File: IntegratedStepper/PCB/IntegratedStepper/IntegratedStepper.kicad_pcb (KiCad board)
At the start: 2 copper layers, 42 x 42 mm, 82 parts, among them IC1 DRV8844PWPR, IC2 SN65HVD230DR, IC3 LMR38020FSQDDARQ1, J1 8P8C, J2 8P8C, J3 Screw_Terminal_01x02, J4 Screw_Terminal_01x02, J5 Conn_01x05_Socket, P1 USB_C_Plug, Q1 SS8050-G, Q2 SS8050-G, U1 ESP32-WROOM-32E, U2 AS5048A, U3 CP2102N-Axx-xQFN28

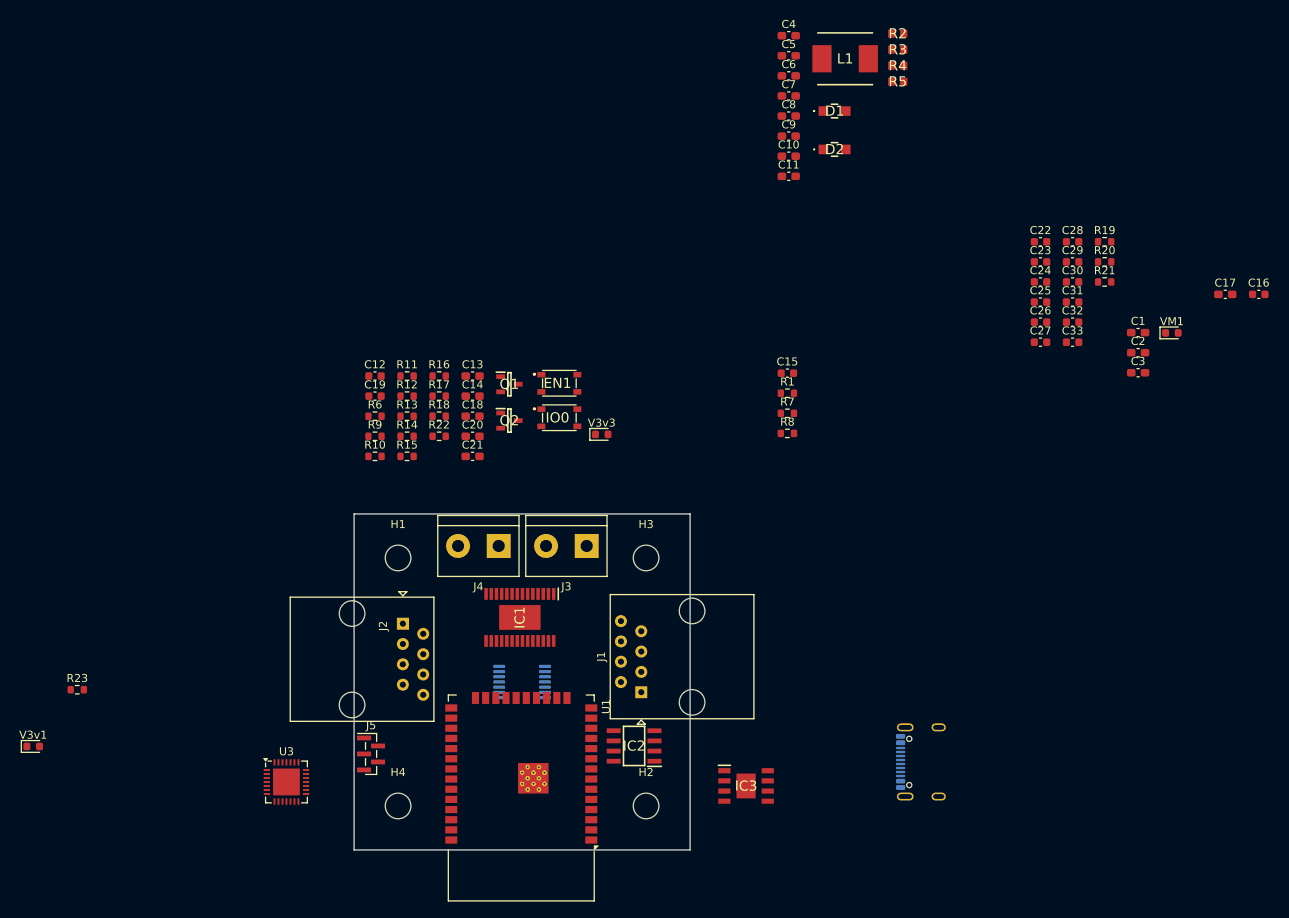
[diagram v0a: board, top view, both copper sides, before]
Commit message: Add intermediate layout + routing to integrated stepper
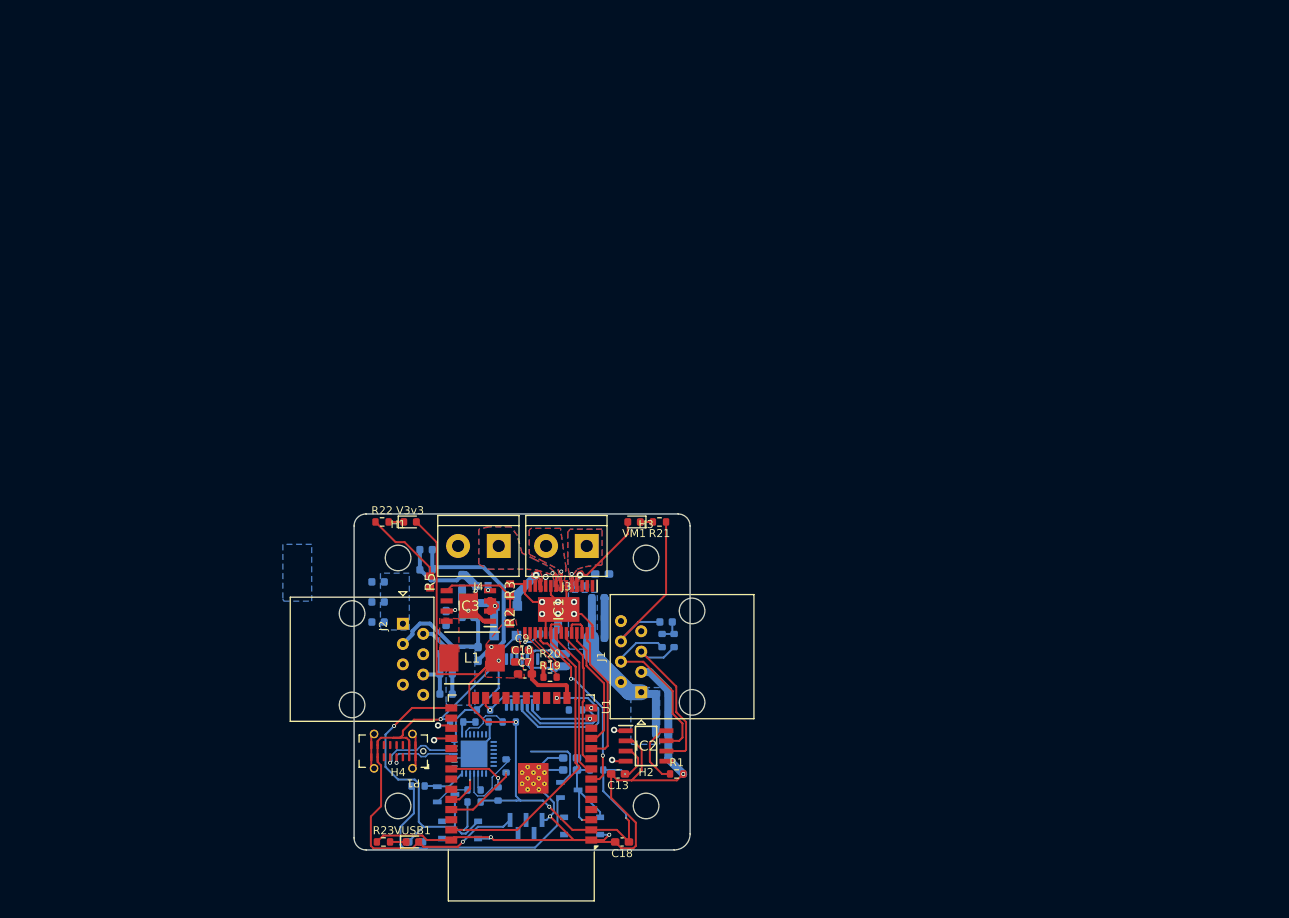
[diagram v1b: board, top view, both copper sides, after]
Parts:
- C1, C11, C12, C14, C15, C16, C17, C19, C2, C20, C21, C22, C23, C24, C25, C26, C27, C28, C29, C3, C30, C31, C32, C33, C4, C5, C6, C8, D1, D2, EN1, IO0, J5, Q1, Q2, R10, R11, R12, R13, R14, R15, R16, R17, R18, R4, R6, R7, R8, R9, U3: moved to B.Cu
- P1: footprint Connector_USB:USB_C_Receptacle_GCT_USB4105-xx-A_16P_TopMnt_Horizontal -> Connector_USB:USB_C_Receptacle_G-Switch_GT-USB-7051x; moved to F.Cu
- moved C16 97.9 mm to (126.5, 118.3), turned to 90 degrees
- moved C17 95.6 mm to (125.0, 118.4), turned to 90 degrees
- moved C31 93.6 mm to (103.0, 108.5), turned to 180 degrees
- moved C32 93.6 mm to (103.0, 111.0), turned to 180 degrees
- moved C33 93.6 mm to (103.0, 113.5), turned to 180 degrees
- moved L1 88.2 mm to (114.8, 118.0)
- moved R19 88.1 mm to (124.5, 120.4)
- moved R2 87.6 mm to (119.5, 113.0), turned to 90 degrees
- moved C26 86.3 mm to (111.5, 120.0), turned to 180 degrees
- moved C27 86.3 mm to (111.5, 122.5), turned to 180 degrees
- moved C25 86.3 mm to (111.5, 117.5), turned to 180 degrees
- moved R20 85.7 mm to (124.5, 118.9)
- moved R5 85.6 mm to (109.5, 108.5), turned to 90 degrees
- moved R4 83.2 mm to (116.0, 109.0), turned to 180 degrees
- moved R3 83.1 mm to (119.5, 109.5), turned to 90 degrees
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- renumbered V3v1 to VUSB1
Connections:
- net /CAN_Transciever/RX renamed /CAN_Transciever/CAN_RX
- net /CAN_Transciever/TX renamed /CAN_Transciever/CAN_TX
- C10 pad 2: VS -> GND
- C22 pad 2: VS -> GND
- C23 pad 2: VS -> GND
- C24 pad 2: VS -> GND
- C25 pad 2: VS -> GND
- C26 pad 2: VS -> GND
- C27 pad 2: VS -> GND
- C28 pad 2: VS -> GND
- C29 pad 2: VS -> GND
- C3 pad 1: VS -> GND
- C30 pad 2: VS -> GND
- C31 pad 2: VS -> GND
- C32 pad 2: VS -> GND
- C33 pad 2: VS -> GND
- C4 pad 1: VS -> GND
- C5 pad 1: VS -> GND
- C6 pad 1: VS -> GND
- C7 pad 2: VS -> GND
- C8 pad 2: VS -> GND
- C9 pad 2: VS -> GND
- IC1 pad 14: VS -> GND
- IC1 pad 28: VS -> GND
- IC1 pad 29: VS -> GND
- IC1 pad 6: VS -> GND
- IC1 pad 9: VS -> GND
- IC3 pad 1: VS -> GND
- IC3 pad 9: VS -> GND
- J1 pad 3: VS -> GND
- J1 pad 6: VS -> GND
- J2 pad 3: VS -> GND
- J2 pad 6: VS -> GND
- R21 pad 1: VS -> GND
- R3 pad 2: VS -> GND
- R4 pad 2: VS -> GND
- R5 pad 2: VS -> GND
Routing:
- net GND: track 0.00 -> 253.1 mm, vias 0 -> 13
- net 3V3_VCC: track 0.00 -> 135.1 mm, vias 0 -> 6
- net /3V3_VReg/V_USB: track 0.00 -> 62.6 mm, vias 0 -> 2
- net VCC: track 0.00 -> 57.3 mm, vias 0 -> 2
- net CANH: track 0.00 -> 53.6 mm
- net CANL: track 0.00 -> 48.6 mm
- net /DRV8844/EN3: track 0.00 -> 44.5 mm, vias 0 -> 1
- net IO0: track 0.00 -> 38.9 mm, vias 0 -> 1
- net Net-(Q1-B): track 0.00 -> 32.8 mm
- net /CAN_Transciever/CAN_RX: track 0.00 -> 29.3 mm, vias 0 -> 2
- net /CAN_Transciever/CAN_TX: track 0.00 -> 25.5 mm, vias 0 -> 2
- net /DRV8844/NFAULT: track 0.00 -> 23.2 mm, vias 0 -> 2
- net /DRV8844/IN4: track 0.00 -> 19.2 mm
- net /ESP32_MCU/M_MOSI: track 0.00 -> 18.8 mm, vias 0 -> 1
- net /DRV8844/IN3: track 0.00 -> 17.5 mm
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- added copper zone on B.Cu, net /DRV8844/OUT1
- added copper zone on F.Cu, net /DRV8844/OUT1
- added copper zone on B.Cu, net /DRV8844/OUT2
- added copper zone on F.Cu, net /DRV8844/OUT2
- added copper zone on B.Cu, net /DRV8844/OUT3
- added copper zone on F.Cu, net /DRV8844/OUT3
- added copper zone on In1.Cu, net /DRV8844/OUT4
- added copper zone on In2.Cu, net /DRV8844/OUT4
- added copper zone on F.Cu, net 3V3_VCC
- added copper zone on F.Cu, net Net-(IC3-SW)
- added copper zone on B.Cu, net VCC
- added copper zone on F.Cu, net VCC
- added copper zone on In1.Cu, net VCC
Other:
- outline, holes or cut-outs redrawn
- copper layers 2 -> 4

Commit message: Add final layout + 3D models
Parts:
- removed P1: USB_C_Plug, Connector_USB:USB_C_Receptacle_G-Switch_GT-USB-7051x
- added USBC1: TYPE-C 3.1_C168690, easyeda2kicad:USB-C-SMD_TYPE-C-USB-3, F.Cu at (104.9, 129.8)
- moved R17 1.25 mm to (119.2, 135.0)
- moved R11 0.25 mm to (119.2, 131.5)
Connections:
- net /3V3_VReg/V_USB renamed V_USB
- IC1 pad 24: /DRV8844/EN1 -> /DRV8844/EN2
- IC1 pad 26: /DRV8844/EN1 -> /DRV8844/EN2
- R17 pad 2: /DRV8844/EN1 -> /DRV8844/EN3
- R18 pad 2: /DRV8844/EN3 -> /DRV8844/EN2
- U1 pad 31: /DRV8844/EN1 -> /DRV8844/EN3
- U1 pad 37: /DRV8844/EN3 -> /DRV8844/EN2
- U3 pad 4: /ESP32_MCU/USB_D+ -> USB_D+
- U3 pad 5: /ESP32_MCU/USB_D- -> USB_D-
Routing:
- net /DRV8844/EN2: track 0.00 -> 47.4 mm, vias 0 -> 3
- net GND: track 253.1 -> 289.7 mm, vias 13 -> 16
- net /ESP32_MCU/ENC_IND: track 0.00 -> 23.5 mm, vias 0 -> 1
- net /ESP32_MCU/ENC-: track 0.00 -> 23.2 mm, vias 0 -> 1
- net /ESP32_MCU/ENC+: track 0.00 -> 19.3 mm, vias 0 -> 3
- net RTS: track 11.4 -> 23.0 mm
- net USB_D+: track 0.00 -> 11.2 mm, vias 0 -> 1
- net /DRV8844/EN1: track 10.8 -> 0.00 mm, vias 1 -> 0
- net USB_D-: track 0.00 -> 10.5 mm, vias 0 -> 2
- net /ESP32_MCU/USB_D-: track 9.60 -> 0.00 mm, vias 1 -> 0
- net /DRV8844/EN3: track 44.5 -> 35.7 mm
- net /ESP32_MCU/USB_D+: track 8.50 -> 0.00 mm, vias 1 -> 0
- net IO0: track 38.9 -> 44.0 mm
- net 3V3_VCC: track 135.1 -> 138.6 mm, vias 6 -> 7
- net Net-(IC3-PG): track 0.00 -> 3.01 mm, vias 0 -> 2
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- added copper zone on In1.Cu, net 3V3_VCC
- added copper zone on B.Cu, net GND
- added copper zone on F.Cu, net GND
- added copper zone on In2.Cu, net GND
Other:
- board size 42 x 42 mm -> 42 x 42.5 mm

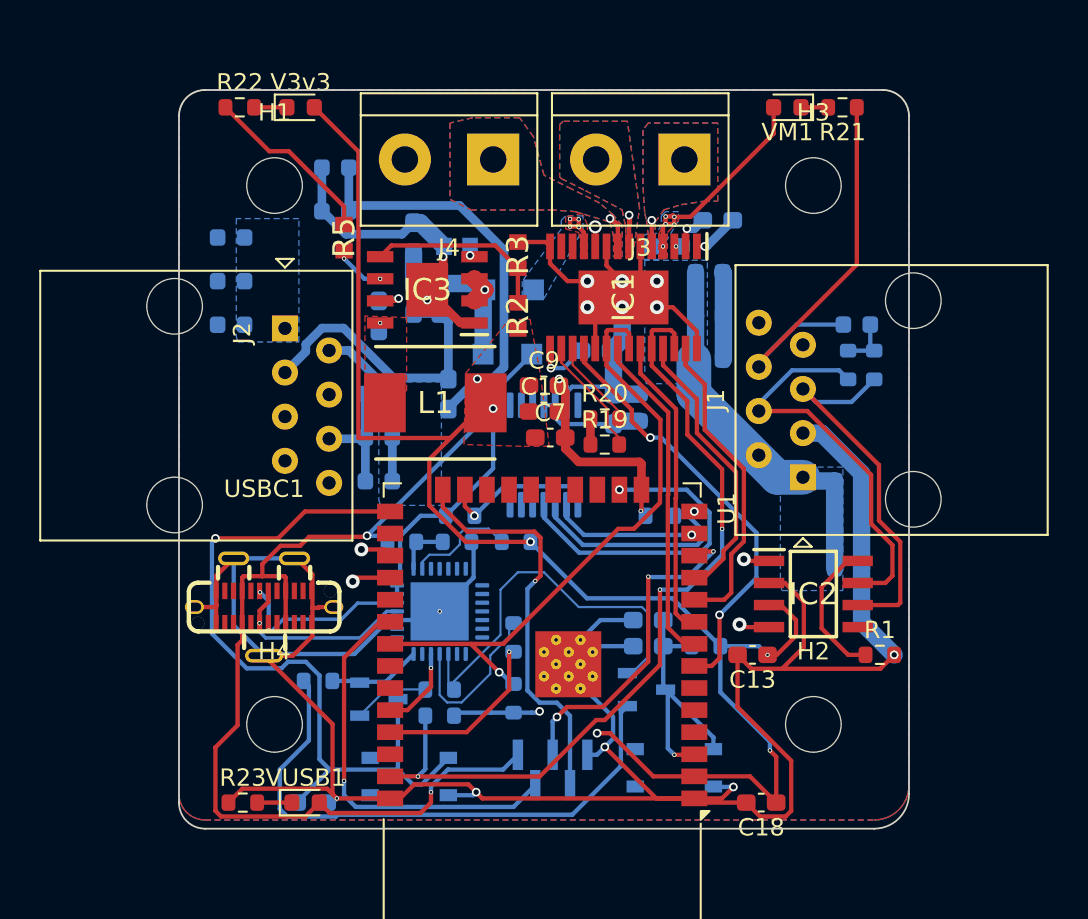
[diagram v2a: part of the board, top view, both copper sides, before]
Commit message: add changes for instock parts
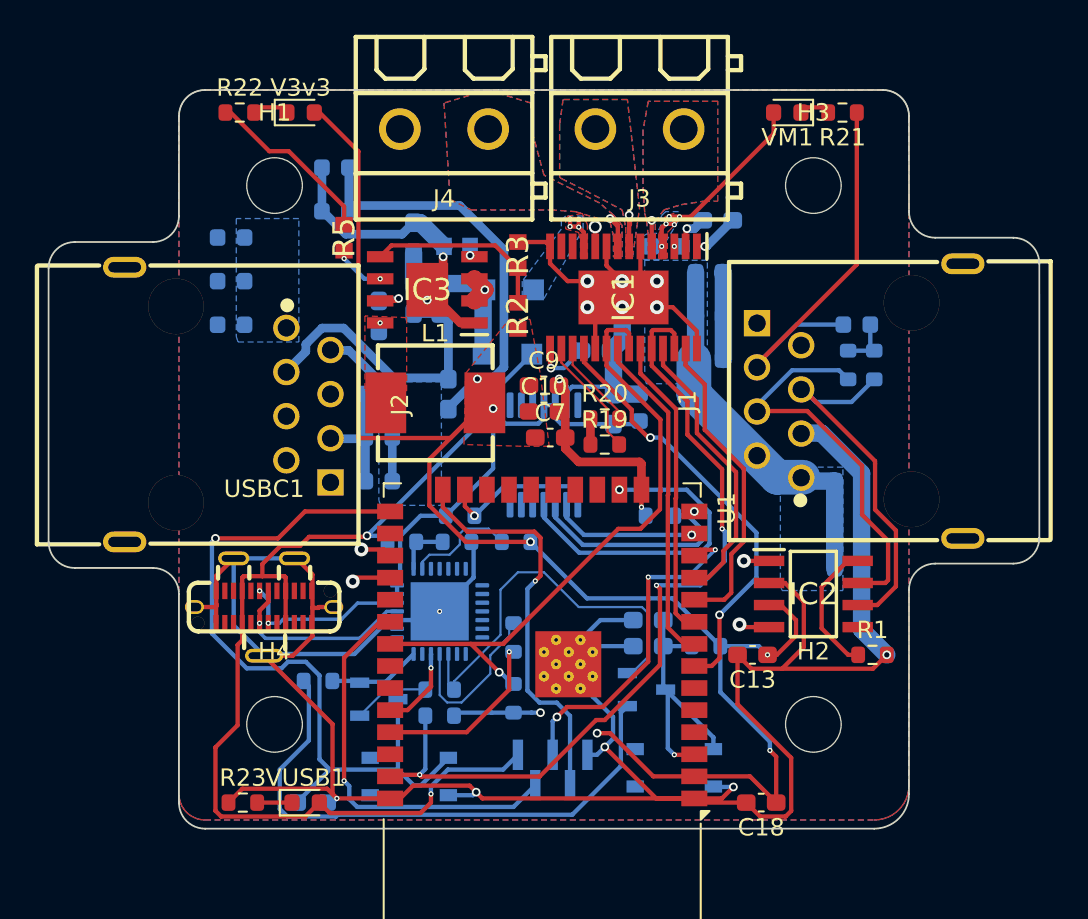
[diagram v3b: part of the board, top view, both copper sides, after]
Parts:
- J1, J2: footprint Connector_RJ:RJ45_Amphenol_54602-x08_Horizontal -> easyeda2kicad:RJ45-TH_KH-RJ45-58-8P8C
- J3, J4: footprint TerminalBlock:TerminalBlock_bornier-2_P5.08mm -> easyeda2kicad:CONN-TH_P5.08_KF128-5.08-2P
- L1: footprint SamacSys_Parts:INDPM6965X300N -> easyeda2kicad:IND-SMD_L7.2-W6.6_GPSR07X0
- moved J2 5.49 mm to (102.8, 118.1)
- moved J1 5.47 mm to (139.2, 117.9)
- moved J4 3.33 mm to (115.2, 102.2)
- moved J3 3.12 mm to (126.5, 102.2)
- moved R1 0.42 mm to (139.9, 132.5)
- moved R21 0.30 mm to (138.2, 101.3)
- moved R22 0.30 mm to (103.5, 101.3)
- moved V3v3 0.30 mm to (107.0, 101.3)
- moved VM1 0.30 mm to (135.0, 101.3)
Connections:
- net /DRV8844/EN2 renamed /DRV8844/EN1
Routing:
- net 3V3_VCC: track 138.6 -> 142.8 mm
- net CANH: track 53.6 -> 52.7 mm
- net GND: track 289.7 -> 288.8 mm
- net /DRV8844/EN1: track 47.4 -> 48.2 mm
- net USB_D-: track 10.5 -> 9.97 mm
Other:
- board size 42 x 42.5 mm -> 57 x 42.5 mm

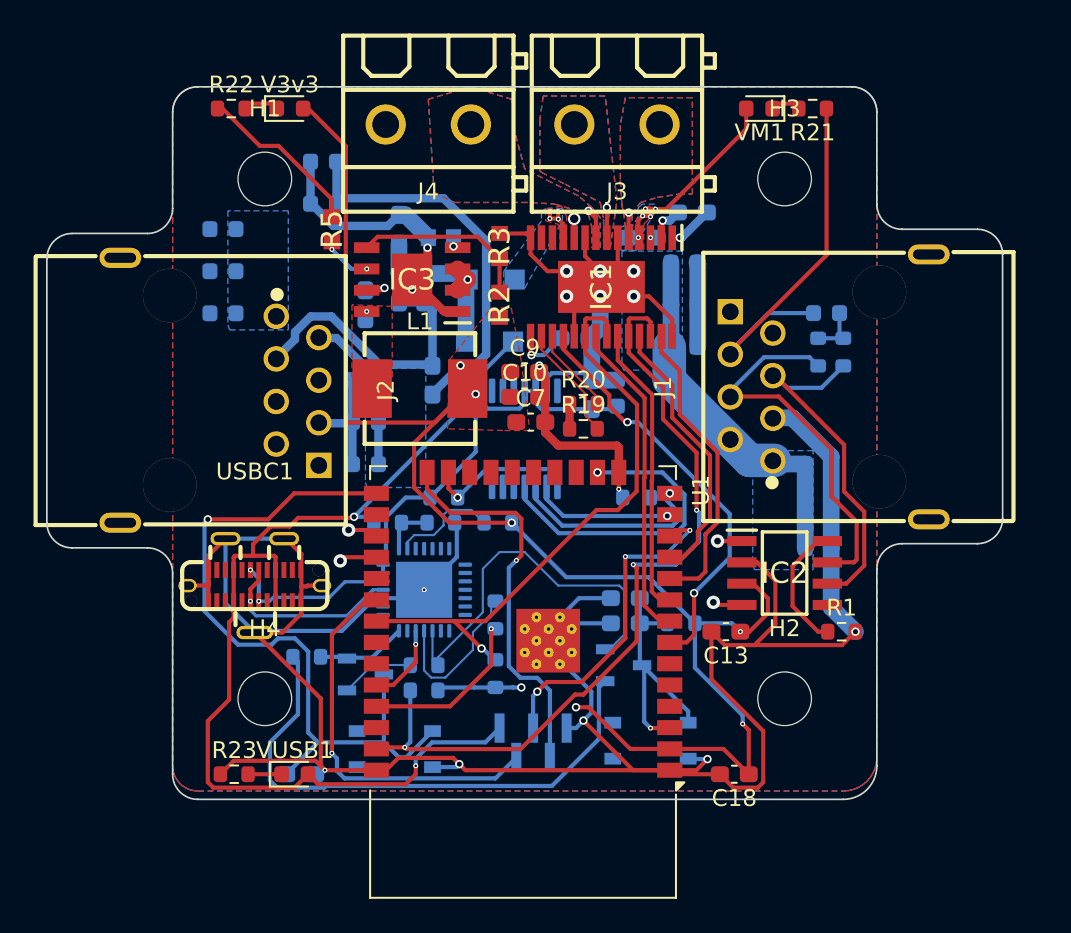
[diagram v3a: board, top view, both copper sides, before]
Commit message: update with more in stock parts
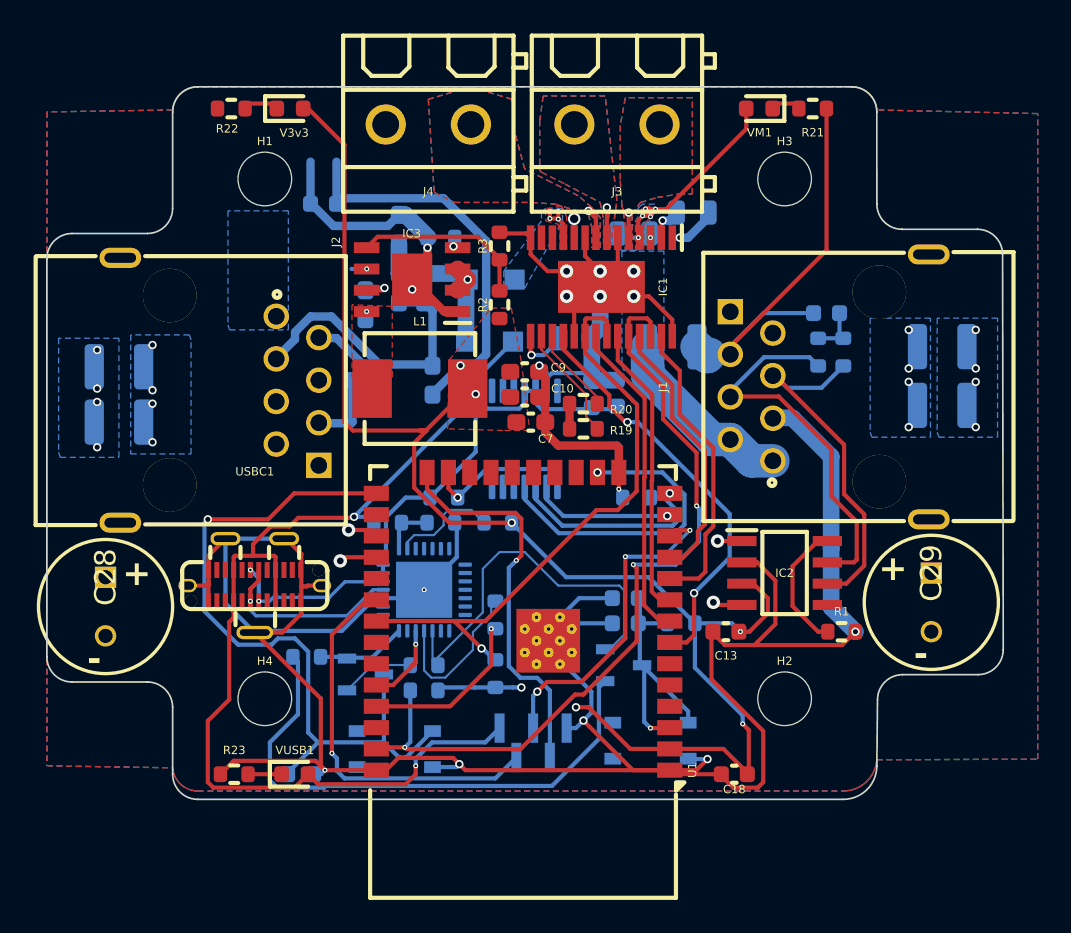
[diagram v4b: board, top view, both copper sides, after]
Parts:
- removed C12, C30, C31, C32, C33: 10uF, Capacitor_SMD:C_0603_1608Metric
- removed R5: 154k, SamacSys_Parts:RESC1608X55N
- C1, C2, C3: footprint Capacitor_SMD:C_0603_1608Metric_Pad1.08x0.95mm_HandSolder -> Capacitor_SMD:C_0805_2012Metric
- C13, C14, C17, C18, C20, C21: footprint Capacitor_SMD:C_0603_1608Metric_Pad1.08x0.95mm_HandSolder -> Capacitor_SMD:C_0603_1608Metric
- C22, C23, C24, C26, C27: footprint Capacitor_SMD:C_0603_1608Metric -> Capacitor_SMD:C_1210_3225Metric
- C28, C29: value 22uF -> 100uF; footprint Capacitor_SMD:C_0603_1608Metric -> SamacSys_Parts:CAPPRD350W65D800H1650; moved to F.Cu
- R2, R3, R4: footprint SamacSys_Parts:RESC1608X55N -> Resistor_SMD:R_0603_1608Metric
- moved C28 42.5 mm to (96.0, 129.2), turned to -90 degrees
- moved C23 16.5 mm to (145.9, 119.0)
- moved C24 16.2 mm to (145.9, 115.5)
- moved C26 15.1 mm to (96.8, 116.7)
- moved C27 14.9 mm to (96.8, 120.0)
- moved C29 7.84 mm to (145.2, 129.0), turned to -90 degrees
- moved C22 0.70 mm to (129.8, 115.5)
- moved C2 0.56 mm to (127.5, 108.8)
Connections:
- net /DRV8844/EN1 renamed /DRV8844/EN2
- net /DRV8844/EN3 renamed /DRV8844/EN4
- IC3 pad 6: Net-(IC3-PG) -> unconnected-(IC3-PG-Pad6)
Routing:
- net GND: track 288.8 -> 272.2 mm, vias 16 -> 24
- net VCC: track 54.3 -> 39.3 mm, vias 9 -> 17
- net Net-(IC3-PG): track 3.01 -> 0.00 mm, vias 2 -> 0
- net 3V3_VCC: track 142.8 -> 140.0 mm
- net unconnected-(IC3-PG-Pad6): track 0.00 -> 0.91 mm, vias 0 -> 1
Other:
- outline, holes or cut-outs redrawn
- board text added: "+"
- board text added: "-"
- board text added: "O1"
- board text added: "O2"
- board text added: "O3"
- board text added: "O4"
